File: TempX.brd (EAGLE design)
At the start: 10.2 x 10.2 mm, 6 parts, among them U1 TMP36

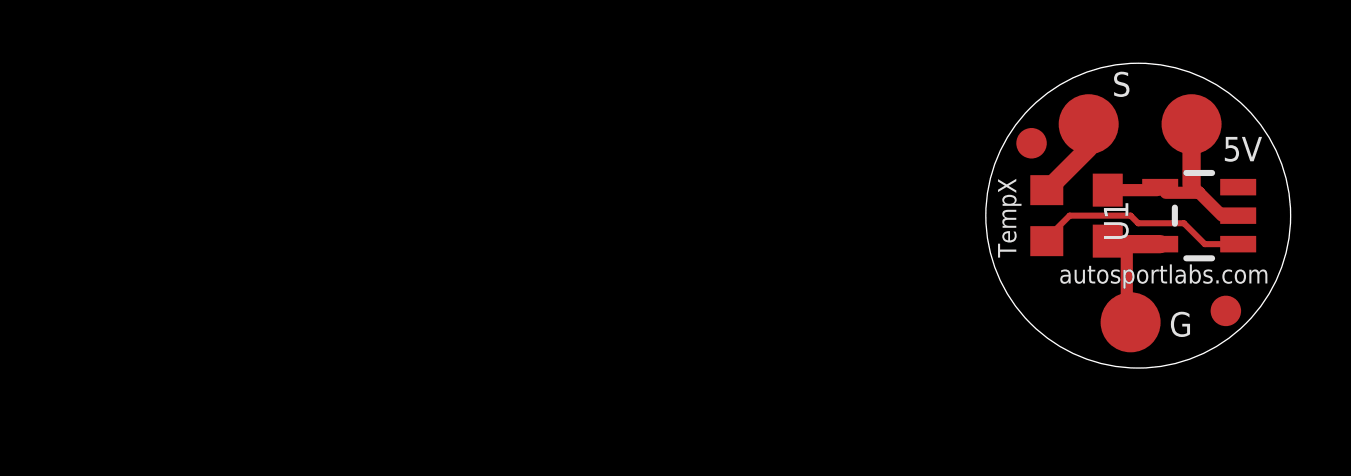
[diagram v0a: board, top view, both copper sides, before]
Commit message: change layout to rectangle
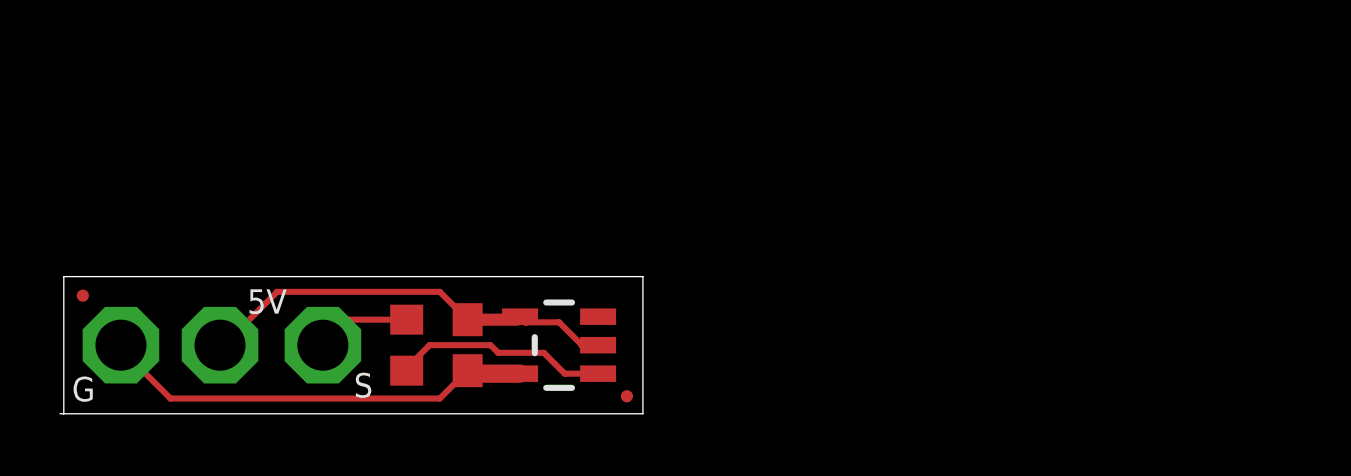
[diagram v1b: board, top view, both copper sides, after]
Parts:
- 5V, G, S: value TPSQTP20R -> TPSQPAD1-17; device testpad:TP20R -> testpad:P1-17
- moved G 33.7 mm to (1.91, 2.29)
- moved 5V 33.2 mm to (5.21, 2.29)
- moved S 26.6 mm to (8.64, 2.29)
- moved C11 21.8 mm to (13.5, 2.29)
- moved R1 21.8 mm to (11.4, 2.29)
- moved U1 21.8 mm to (16.5, 2.29)
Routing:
- net C1: track 4.41 -> 14.5 mm
- net 5V: track 7.27 -> 14.3 mm
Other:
- board size 10.2 x 10.2 mm -> 19.4 x 4.6 mm
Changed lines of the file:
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@@
 <setting verticaltext="up"/>
 </settings>
-<grid distance="0.005" unitdist="inch" unit="inch" style="lines" multiple="1" display="no" altdistance="0.025" altunitdist="inch" altunit="inch"/>
+<grid distance="0.001" unitdist="inch" unit="inch" style="lines" multiple="1" display="no" altdistance="0.025" altunitdist="inch" altunit="inch"/>
 <layers>
 <layer number="1" name="Top" color="4" fill="1" visible="yes" active="yes"/>
@@
 <board>
 <plain>
-<text x="40.1828" y="4.953" size="0.6096" layer="21" font="vector" rot="R180">autosportlabs.com</text>
-<text x="34.3662" y="8.763" size="0.6096" layer="22" font="vector" rot="MR180">Rev A</text>
-<text x="31.75" y="5.207" size="0.6096" layer="21" rot="R90">TempX</text>
-<circle x="35.814" y="6.604" radius="5.08" width="0.0254" layer="20"/>
-<circle x="32.258" y="9.017" radius="0.508" width="0" layer="1"/>
-<circle x="32.258" y="9.017" radius="0.5588" width="0" layer="29"/>
-<circle x="38.735" y="3.429" radius="0.508" width="0" layer="1"/>
-<circle x="38.735" y="3.429" radius="0.5588" width="0" layer="29"/>
+<text x="10.0838" y="1.016" size="0.6096" layer="22" font="vector" rot="MR180">autosportlabs.com</text>
+<text x="14.9352" y="4.191" size="0.6096" layer="22" font="vector" rot="MR180">Rev A</text>
+<text x="18.923" y="3.81" size="0.6096" layer="22" rot="MR270">TempX</text>
+<circle x="0.635" y="3.937" radius="0.2032" width="0" layer="1"/>
+<circle x="0.635" y="3.937" radius="0.2286" width="0" layer="29"/>
+<circle x="18.7706" y="0.5842" radius="0.2032" width="0" layer="1"/>
+<circle x="18.7706" y="0.5842" radius="0.2286" width="0" layer="29"/>
+<wire x1="-0.127" y1="0" x2="0" y2="0" width="0" layer="20"/>
+<wire x1="0" y1="0" x2="19.304" y2="0" width="0" layer="20"/>
+<wire x1="19.304" y1="0" x2="19.304" y2="4.572" width="0" layer="20"/>
+<wire x1="19.304" y1="4.572" x2="0" y2="4.572" width="0" layer="20"/>
+<wire x1="0" y1="4.572" x2="0" y2="0" width="0" layer="20"/>
 </plain>
 <attributes>
@@
 </autorouter>
 <elements>
-<element name="U1" library="TMP36" package="SOT-23" value="TMP36" x="37.846" y="6.604" smashed="yes" rot="R90">
-<attribute name="NAME" x="34.671" y="7.112" size="0.8128" layer="25" rot="R270"/>
+<element name="U1" library="TMP36" package="SOT-23" value="TMP36" x="16.51" y="2.286" smashed="yes" rot="R90"/>
+<element name="R1" library="rcl" package="R0603" value="1K" x="11.43" y="2.286" smashed="yes" rot="R270"/>
+<element name="C11" library="rcl" package="C0603" value="0.1uF" x="13.462" y="2.286" smashed="yes" rot="R270"/>
+<element name="S" library="testpad" package="P1-17" value="TPSQPAD1-17" x="8.636" y="2.286" smashed="yes">
+<attribute name="TP_SIGNAL_NAME" value="" x="8.636" y="-0.254" size="1" layer="37"/>
+<attribute name="NAME" x="9.668" y="0.542" size="0.8128" layer="25"/>
 </element>
-<element name="R1" library="rcl" package="R0603" value="1K" x="32.766" y="6.604" smashed="yes" rot="R270"/>
-<element name="C11" library="rcl" package="C0603" value="0.1uF" x="34.798" y="6.604" smashed="yes" rot="R270"/>
-<element name="S" library="testpad" package="TP20R" value="TPSQTP20R" x="34.163" y="9.652" smashed="yes">
-<attribute name="TP_SIGNAL_NAME" value="" x="34.163" y="7.112" size="1" layer="37"/>
-<attribute name="NAME" x="34.941" y="10.575" size="0.8128" layer="25"/>
+<element name="5V" library="testpad" package="P1-17" value="TPSQPAD1-17" x="5.207" y="2.286" smashed="yes">
+<attribute name="TP_SIGNAL_NAME" value="" x="5.207" y="-0.254" size="1" layer="37"/>
+<attribute name="NAME" x="6.112" y="3.336" size="0.8128" layer="25"/>
 </element>
-<element name="5V" library="testpad" package="TP20R" value="TPSQTP20R" x="37.592" y="9.652" smashed="yes">
-<attribute name="TP_SIGNAL_NAME" value="" x="37.592" y="7.112" size="1" layer="37"/>
-<attribute name="NAME" x="38.624" y="8.416" size="0.8128" layer="25"/>
-</element>
-<element name="G" library="testpad" package="TP20R" value="TPSQTP20R" x="35.56" y="3.048" smashed="yes">
-<attribute name="TP_SIGNAL_NAME" value="" x="35.56" y="0.508" size="1" layer="37"/>
-<attribute name="NAME" x="36.846" y="2.574" size="0.8128" layer="25"/>
+<element name="G" library="testpad" package="P1-17" value="TPSQPAD1-17" x="1.905" y="2.286" smashed="yes">
+<attribute name="TP_SIGNAL_NAME" value="" x="1.905" y="-0.254" size="1" layer="37"/>
+<attribute name="NAME" x="0.27" y="0.415" size="0.8128" layer="25"/>
 </element>
 </elements>
@@
 <contactref element="R1" pad="1"/>
 <contactref element="S" pad="TP"/>
-<wire x1="34.163" y1="9.652" x2="34.163" y2="8.851" width="0.4064" layer="1"/>
-<wire x1="34.163" y1="8.851" x2="32.766" y2="7.454" width="0.6096" layer="1"/>
+<wire x1="11.43" y1="3.136" x2="9.486" y2="3.136" width="0.2032" layer="1"/>
+<wire x1="9.486" y1="3.136" x2="8.636" y2="2.286" width="0.2032" layer="1"/>
 </signal>
 <signal name="N$2">
 <contactref element="R1" pad="2"/>
 <contactref element="U1" pad="1"/>
-<wire x1="33.528" y1="6.604" x2="32.766" y2="5.842" width="0.2032" layer="1"/>
-<wire x1="32.766" y1="5.842" x2="32.766" y2="5.754" width="0.254" layer="1"/>
-<wire x1="33.528" y1="6.604" x2="35.56" y2="6.604" width="0.2032" layer="1"/>
-<wire x1="35.56" y1="6.604" x2="35.814" y2="6.35" width="0.2032" layer="1"/>
-<wire x1="35.814" y1="6.35" x2="37.338" y2="6.35" width="0.2032" layer="1"/>
-<wire x1="37.338" y1="6.35" x2="38.034" y2="5.654" width="0.2032" layer="1"/>
-<wire x1="38.034" y1="5.654" x2="39.1461" y2="5.654" width="0.2032" layer="1"/>
+<wire x1="12.192" y1="2.286" x2="11.43" y2="1.524" width="0.2032" layer="1"/>
+<wire x1="11.43" y1="1.524" x2="11.43" y2="1.436" width="0.254" layer="1"/>
+<wire x1="12.192" y1="2.286" x2="14.224" y2="2.286" width="0.2032" layer="1"/>
+<wire x1="14.224" y1="2.286" x2="14.478" y2="2.032" width="0.2032" layer="1"/>
+<wire x1="14.478" y1="2.032" x2="16.002" y2="2.032" width="0.2032" layer="1"/>
+<wire x1="16.002" y1="2.032" x2="16.698" y2="1.336" width="0.2032" layer="1"/>
+<wire x1="16.698" y1="1.336" x2="17.8101" y2="1.336" width="0.2032" layer="1"/>
 </signal>
 <signal name="5V">
@@
 <contactref element="U1" pad="4"/>
 <contactref element="U1" pad="2"/>
-<wire x1="36.5459" y1="7.554" x2="36.4459" y2="7.454" width="0.3048" layer="1"/>
-<wire x1="36.4459" y1="7.454" x2="34.798" y2="7.454" width="0.4064" layer="1"/>
-<wire x1="36.4799" y1="7.62" x2="36.5459" y2="7.554" width="0.254" layer="1"/>
-<wire x1="37.846" y1="7.366" x2="36.7339" y2="7.366" width="0.4064" layer="1"/>
-<wire x1="36.7339" y1="7.366" x2="36.5459" y2="7.554" width="0.254" layer="1"/>
-<wire x1="39.1461" y1="6.604" x2="38.608" y2="6.604" width="0.254" layer="1"/>
-<wire x1="38.608" y1="6.604" x2="37.846" y2="7.366" width="0.4064" layer="1"/>
+<wire x1="15.2099" y1="3.236" x2="15.1099" y2="3.136" width="0.3048" layer="1"/>
+<wire x1="15.1099" y1="3.136" x2="13.462" y2="3.136" width="0.4064" layer="1"/>
+<wire x1="15.1439" y1="3.302" x2="15.2099" y2="3.236" width="0.254" layer="1"/>
+<wire x1="16.51" y1="3.048" x2="15.3979" y2="3.048" width="0.2032" layer="1"/>
+<wire x1="15.3979" y1="3.048" x2="15.2099" y2="3.236" width="0.254" layer="1"/>
+<wire x1="17.8101" y1="2.286" x2="17.272" y2="2.286" width="0.254" layer="1"/>
+<wire x1="17.272" y1="2.286" x2="16.51" y2="3.048" width="0.2032" layer="1"/>
 <contactref element="5V" pad="TP"/>
-<wire x1="37.592" y1="9.652" x2="37.592" y2="7.62" width="0.6096" layer="1"/>
-<wire x1="37.592" y1="7.62" x2="37.846" y2="7.366" width="0.4064" layer="1"/>
+<wire x1="5.207" y1="2.286" x2="5.334" y2="2.286" width="0.254" layer="1"/>
+<wire x1="5.334" y1="2.286" x2="7.112" y2="4.064" width="0.2032" layer="1"/>
+<wire x1="7.112" y1="4.064" x2="12.534" y2="4.064" width="0.2032" layer="1"/>
+<wire x1="12.534" y1="4.064" x2="13.462" y2="3.136" width="0.2032" layer="1"/>
 </signal>
 <signal name="C1">
 <contactref element="C11" pad="2"/>
 <contactref element="U1" pad="5"/>
-<wire x1="36.5459" y1="5.654" x2="35.433" y2="5.654" width="0.6096" layer="1"/>
-<wire x1="35.433" y1="5.654" x2="34.898" y2="5.654" width="0.6096" layer="1"/>
-<wire x1="34.898" y1="5.654" x2="34.798" y2="5.754" width="0.254" layer="1"/>
+<wire x1="15.2099" y1="1.336" x2="13.562" y2="1.336" width="0.6096" layer="1"/>
+<wire x1="13.562" y1="1.336" x2="13.462" y2="1.436" width="0.254" layer="1"/>
 <contactref element="G" pad="TP"/>
-<wire x1="35.56" y1="3.048" x2="35.433" y2="3.683" width="0.4064" layer="1"/>
-<wire x1="35.433" y1="3.683" x2="35.433" y2="5.654" width="0.4064" layer="1"/>
+<wire x1="1.905" y1="2.286" x2="1.905" y2="2.159" width="0.254" layer="1"/>
+<wire x1="1.905" y1="2.159" x2="3.556" y2="0.508" width="0.2032" layer="1"/>
+<wire x1="3.556" y1="0.508" x2="12.534" y2="0.508" width="0.2032" layer="1"/>
+<wire x1="12.534" y1="0.508" x2="13.462" y2="1.436" width="0.2032" layer="1"/>
 </signal>
 </signals>
+<errors>
+</errors>
 </board>
 </drawing>
